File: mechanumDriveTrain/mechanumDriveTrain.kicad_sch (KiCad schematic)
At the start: 39 parts, among them IC1 TCAN3414DR, J1 XT30U-M, J2 BM02B-SRSS-TB, J3 5 pin dupont, J4 5 pin dupont, U1 Teensy 4.1, U2 LD1117S50TR_SOT223

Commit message: started routing
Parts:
- IC1: footprint SOIC127P600X175-8N -> Package_SO:SOIC-8_3.9x4.9mm_P1.27mm
- U1: footprint DEV-16771:MODULE_DEV-16771 -> Custom Footprints:Teensy41
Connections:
- net CS1: now also U1.15 (A1); no longer U1.14 (A0)
- net CS2: now also U1.14 (A0); no longer U1.15 (A1)
- net VCC: no longer U4.8 (VM)
- no-connect marks 39 -> 40
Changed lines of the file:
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@@
 	)
 	(no_connect
+		(at 129.54 101.6)
+	)
+	(no_connect
 		(at 184.15 85.09)
 	)
@@
 	(wire
 		(pts
-			(xy 138.43 104.14) (xy 132.08 104.14)
-		)
-		(stroke
-			(width 0)
-			(type default)
-		)
-	)
-	(wire
-		(pts
 			(xy 74.93 99.06) (xy 77.47 99.06)
 		)
@@
 	(wire
 		(pts
-			(xy 132.08 101.6) (xy 129.54 101.6)
-		)
-		(stroke
-			(width 0)
-			(type default)
-		)
-	)
-	(wire
-		(pts
 			(xy 182.88 62.23) (xy 184.15 62.23)
 		)
@@
 	(wire
 		(pts
-			(xy 132.08 104.14) (xy 132.08 101.6)
-		)
-		(stroke
-			(width 0)
-			(type default)
-		)
-	)
-	(wire
-		(pts
 			(xy 224.79 121.92) (xy 224.79 120.65)
 		)
@@
 		)
 	)
+	(global_label "CS2"
+		(shape input)
+		(at 184.15 92.71 180)
+		(fields_autoplaced yes)
+		(effects
+			(font
+				(size 1.27 1.27)
+			)
+			(justify right)
+		)
+		(property "Intersheetrefs" "${INTERSHEET_REFS}"
+			(at 177.4758 92.71 0)
+			(effects
+				(font
+					(size 1.27 1.27)
+				)
+				(justify right)
+				(hide yes)
+			)
+		)
+	)
 	(global_label "OUTB1"
 		(shape input)
@@
 		)
 	)
+	(global_label "CS1"
+		(shape input)
+		(at 184.15 95.25 180)
+		(fields_autoplaced yes)
+		(effects
+			(font
+				(size 1.27 1.27)
+			)
+			(justify right)
+		)
+		(property "Intersheetrefs" "${INTERSHEET_REFS}"
+			(at 177.4758 95.25 0)
+			(effects
+				(font
+					(size 1.27 1.27)
+				)
+				(justify right)
+				(hide yes)
+			)
+		)
+	)
 	(global_label "CANN"
 		(shape input)
@@
 		)
 	)
-	(global_label "CS2"
-		(shape input)
-		(at 184.15 95.25 180)
-		(fields_autoplaced yes)
-		(effects
-			(font
-				(size 1.27 1.27)
-			)
-			(justify right)
-		)
-		(property "Intersheetrefs" "${INTERSHEET_REFS}"
-			(at 177.4758 95.25 0)
-			(effects
-				(font
-					(size 1.27 1.27)
-				)
-				(justify right)
-				(hide yes)
-			)
-		)
-	)
 	(global_label "DIR1"
 		(shape input)
@@
 		)
 	)
-	(global_label "CS1"
-		(shape input)
-		(at 184.15 92.71 180)
-		(fields_autoplaced yes)
-		(effects
-			(font
-				(size 1.27 1.27)
-			)
-			(justify right)
-		)
-		(property "Intersheetrefs" "${INTERSHEET_REFS}"
-			(at 177.4758 92.71 0)
-			(effects
-				(font
-					(size 1.27 1.27)
-				)
-				(justify right)
-				(hide yes)
-			)
-		)
-	)
 	(global_label "EN_OUTB2"
 		(shape input)
@@
 	)
 	(symbol
-		(lib_id "power:VCC")
-		(at 138.43 104.14 0)
-		(unit 1)
-		(exclude_from_sim no)
-		(in_bom yes)
-		(on_board yes)
-		(dnp no)
-		(property "Reference" "#PWR028"
-			(at 138.43 107.95 0)
-			(effects
-				(font
-					(size 1.27 1.27)
-				)
-				(hide yes)
-			)
-		)
-		(property "Value" "VCC"
-			(at 138.43 100.584 0)
-			(effects
-				(font
-					(size 1.27 1.27)
-				)
-			)
-		)
-		(property "Footprint" ""
-			(at 138.43 104.14 0)
-			(effects
-				(font
-					(size 1.27 1.27)
-				)
-				(hide yes)
-			)
-		)
-		(property "Datasheet" ""
-			(at 138.43 104.14 0)
-			(effects
-				(font
-					(size 1.27 1.27)
-				)
-				(hide yes)
-			)
-		)
-		(property "Description" "Power symbol creates a global label with name \"VCC\""
-			(at 138.43 104.14 0)
-			(effects
-				(font
-					(size 1.27 1.27)
-				)
-				(hide yes)
-			)
-		)
-		(pin "1"
-		)
-		(instances
-			(project "mechanumDriveTrain"
-				(path "/150d9912-2987-4a4a-be7d-95dc51376246"
-					(reference "#PWR028")
-					(unit 1)
-				)
-			)
-		)
-	)
-	(symbol
 		(lib_id "Connector:TestPoint")
 		(at 114.3 151.13 270)
@@
 			)
 		)
-		(property "Footprint" "DEV-16771:MODULE_DEV-16771"
+		(property "Footprint" "Custom Footprints:Teensy41"
 			(at 204.47 72.39 0)
 			(effects
@@
 			)
 		)
-		(property "Footprint" "SOIC127P600X175-8N"
+		(property "Footprint" "Package_SO:SOIC-8_3.9x4.9mm_P1.27mm"
 			(at 34.29 -50.47 0)
 			(effects

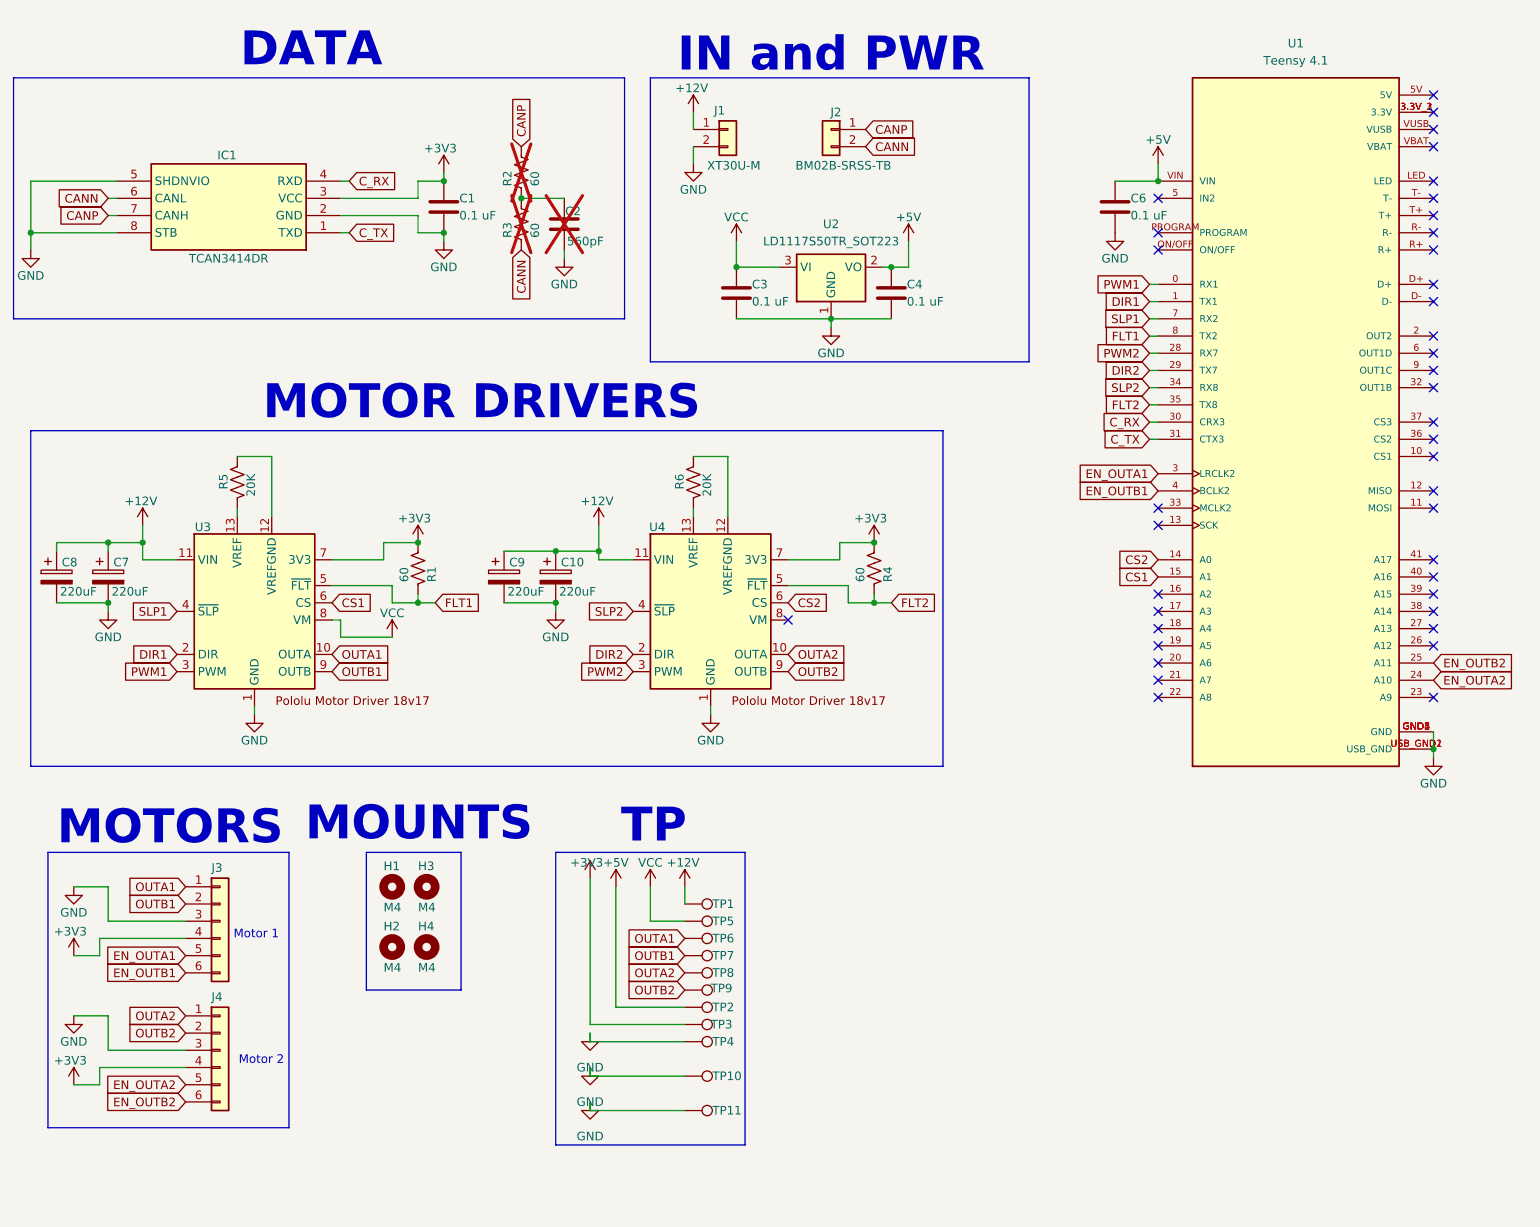
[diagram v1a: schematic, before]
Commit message: revise Teensy footprint, first pass at routing
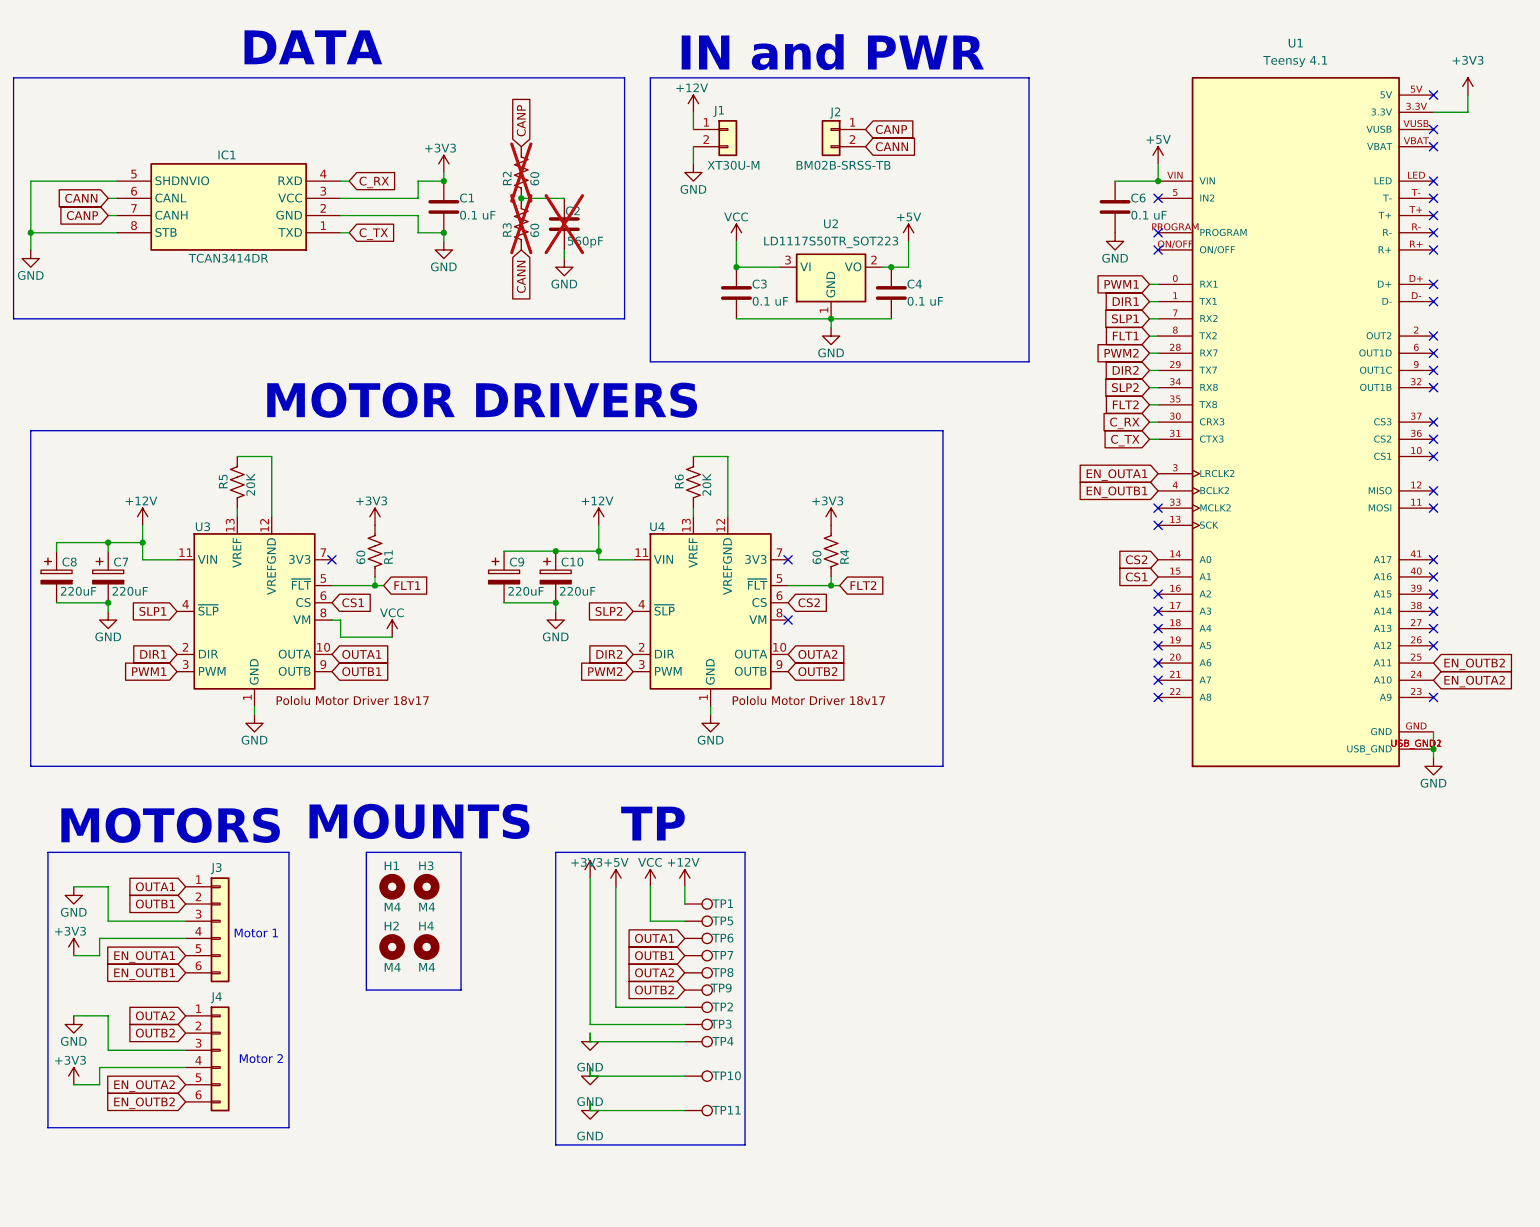
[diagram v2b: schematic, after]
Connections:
- net +3V3: now also U1.3.3V; no longer U3.7 (3V3), U4.7 (3V3)
- net GND: now also U1.GND; no longer U1.GND1 (GND), U1.GND2 (GND), U1.GND3 (GND), U1.GND4 (GND), U1.GND5 (GND)
- no-connect marks 40 -> 41
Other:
- moved on the sheet: R1
